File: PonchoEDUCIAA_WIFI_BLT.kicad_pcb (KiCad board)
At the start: 2 copper layers, 21 parts, among them J1 UART, SW1 Reset, SW2 Boot, U1 ESP32-WROOM

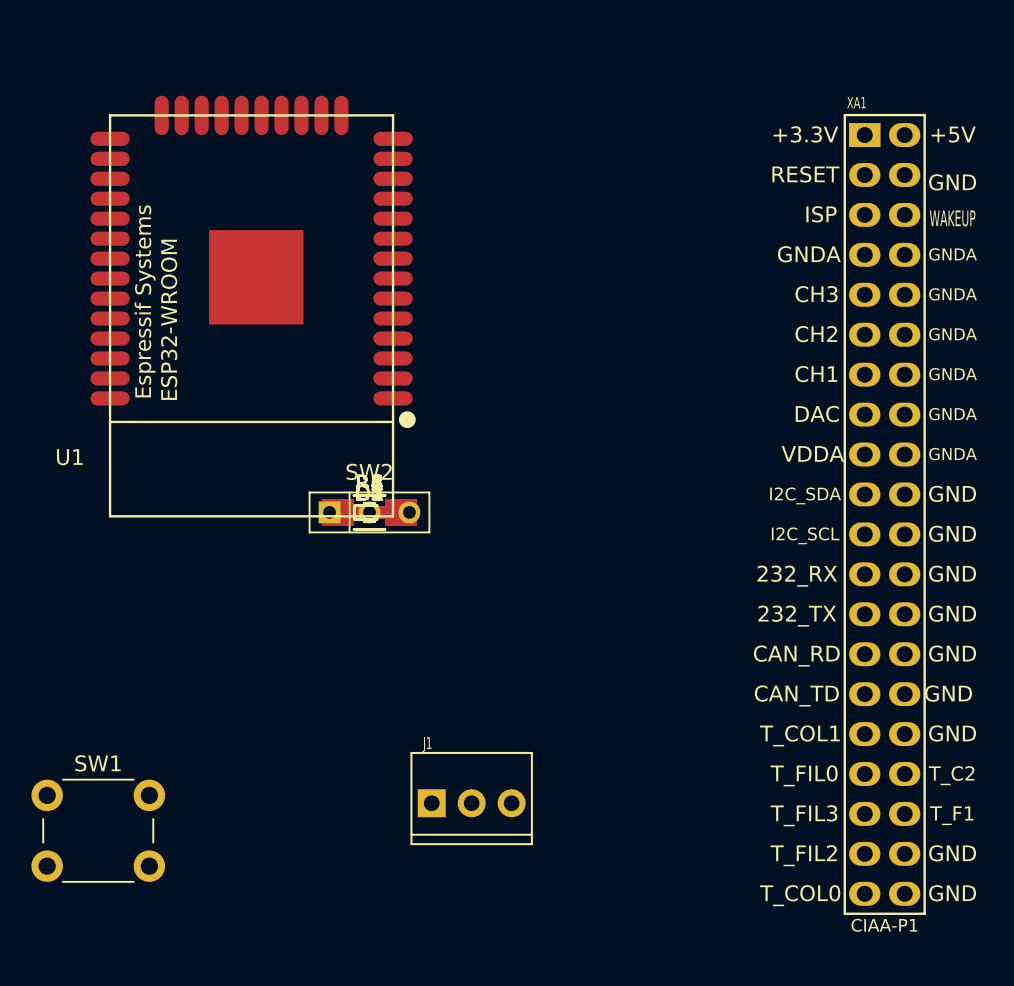
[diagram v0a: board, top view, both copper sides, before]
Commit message: Se distribuyen los componentes en el PCB
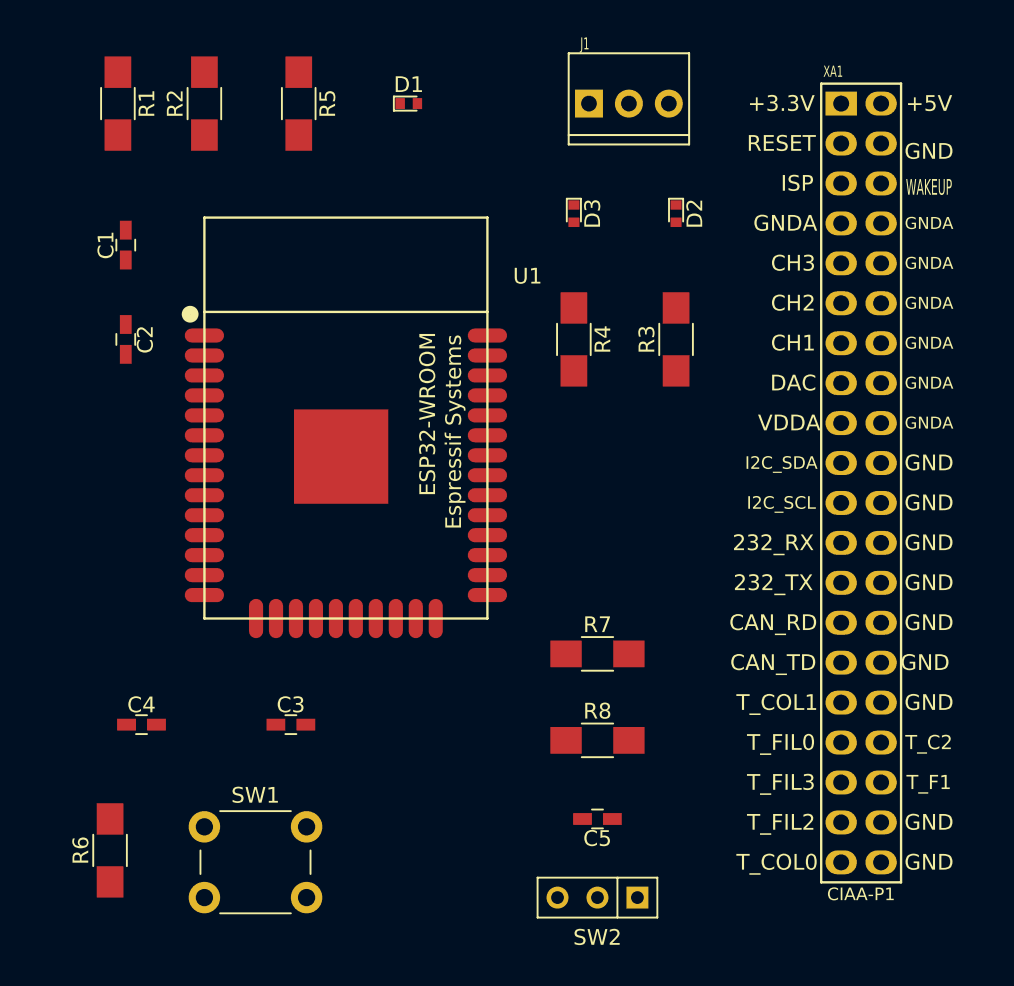
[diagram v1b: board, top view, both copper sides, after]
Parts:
- moved J1 45.6 mm to (165.0, 79.0)
- moved R1 30.5 mm to (132.5, 79.0), turned to 270 degrees
- moved SW2 28.5 mm to (163.0, 129.5), turned to 180 degrees
- moved R2 28.0 mm to (138.0, 79.0), turned to 90 degrees
- moved D2 27.2 mm to (168.0, 86.0), turned to 270 degrees
- moved R6 27.1 mm to (132.0, 126.5), turned to 90 degrees
- moved R5 26.4 mm to (144.0, 79.0), turned to 270 degrees
- moved D1 26.1 mm to (151.0, 79.0)
- moved C5 24.3 mm to (163.0, 124.5), turned to 180 degrees
- moved D3 23.0 mm to (161.5, 86.0), turned to 270 degrees
- moved C1 23.0 mm to (133.0, 88.0), turned to 90 degrees
- moved R3 22.4 mm to (168.0, 94.0), turned to 90 degrees
- moved R8 20.5 mm to (163.0, 119.5)
- moved C4 19.8 mm to (134.0, 118.5)
- moved C2 19.0 mm to (133.0, 94.0), turned to 270 degrees
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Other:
- net class Default: clearance 0.2 -> 0.3; trace_width 0.25 -> 0.3; via_dia 0.6 -> 1.27; via_drill 0.4 -> 0.7
- rule trace_clearance: 0.2 -> 0.3

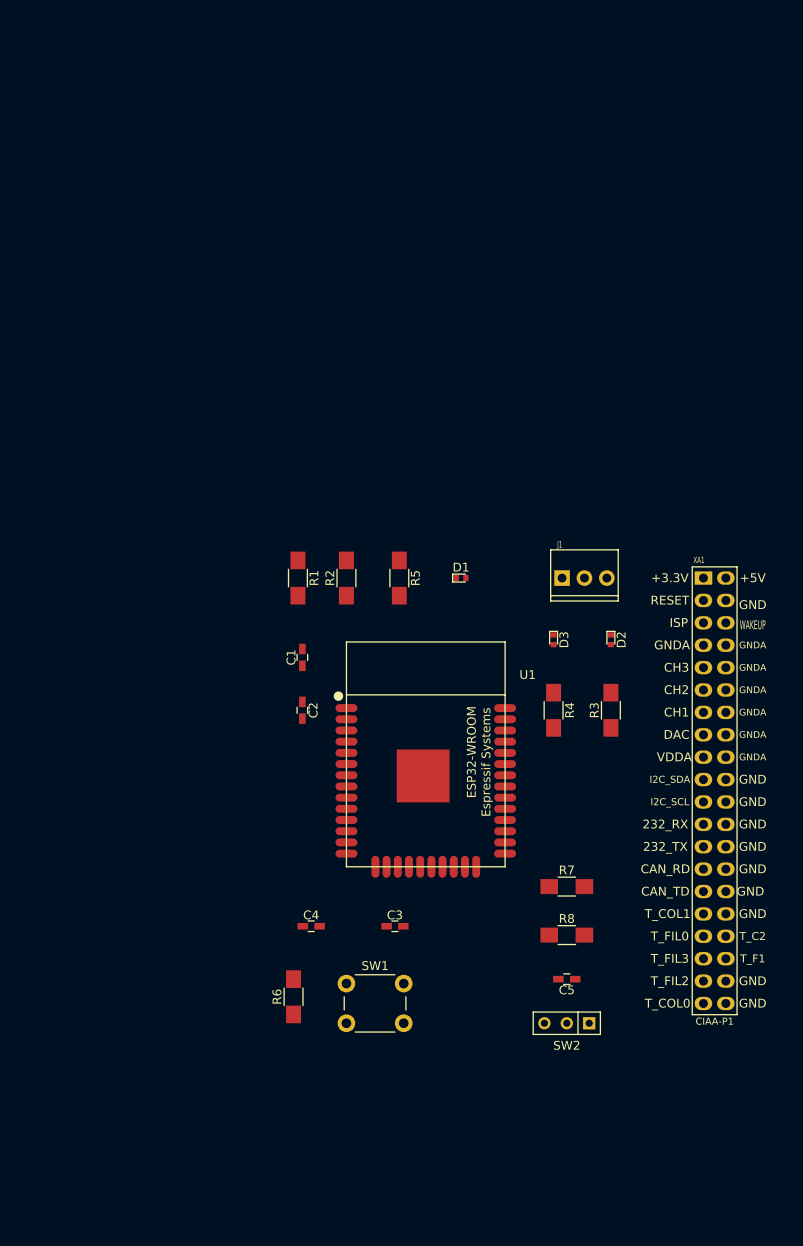
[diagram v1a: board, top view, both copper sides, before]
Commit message: Se agregan modelos 3d al proyecto y datashets de algunos componentes
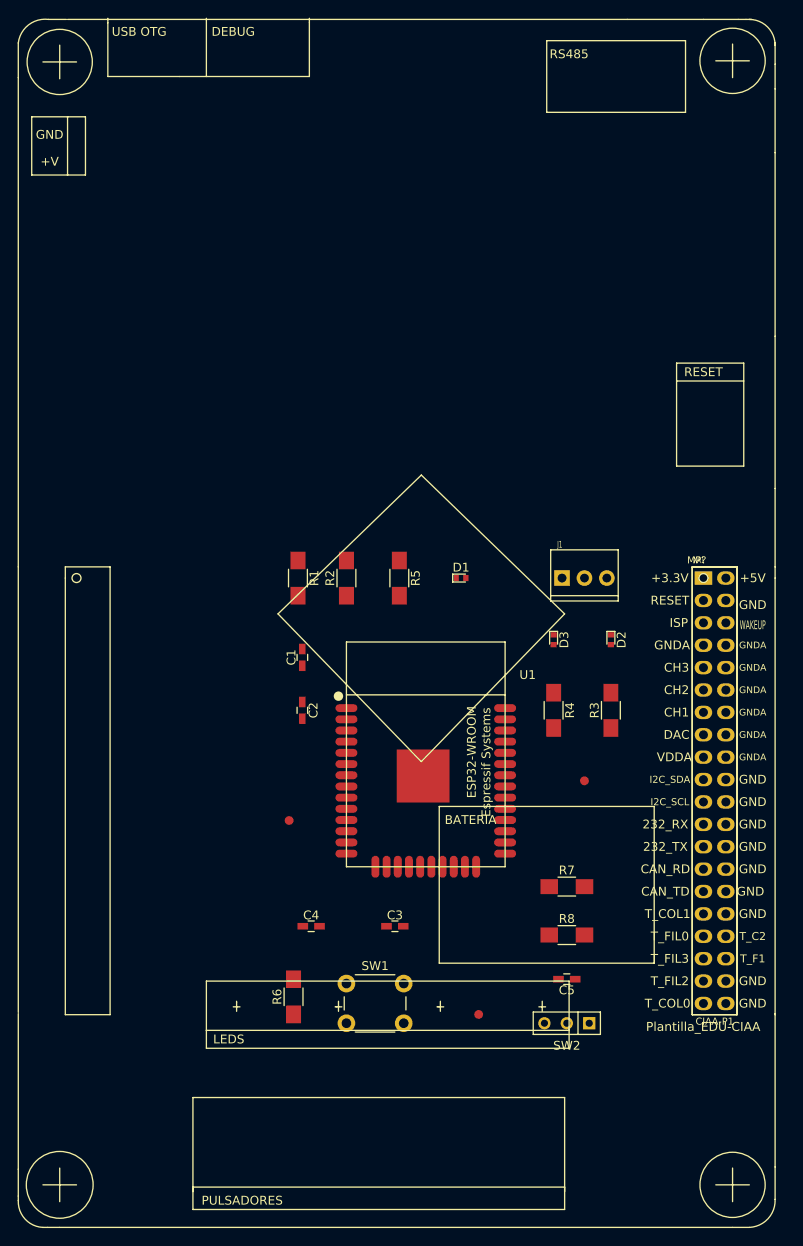
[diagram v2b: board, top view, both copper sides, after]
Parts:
- added F1: FIDUCIAL, PonchoEDUCIAA_WIFI_BLTH:Fiducial_1mm, F.Cu at (153.0, 128.5)
- added F2: FIDUCIAL, PonchoEDUCIAA_WIFI_BLTH:Fiducial_1mm, F.Cu at (131.5, 106.5)
- added F3: FIDUCIAL, PonchoEDUCIAA_WIFI_BLTH:Fiducial_1mm, F.Cu at (165.0, 102.0)
- added MP?: Plantilla_EDU-CIAA, PonchoEDUCIAA_WIFI_BLTH:Plantilla_EDU-CIAA, F.Cu at (178.5, 79.0)
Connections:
- R3 pad 1: Net-(D2-Pad2) -> Net-(J1-Pad1)
- R3 pad 2: Net-(J1-Pad1) -> Net-(D2-Pad2)
- R4 pad 1: Net-(D3-Pad2) -> Net-(J1-Pad2)
- R4 pad 2: Net-(J1-Pad2) -> Net-(D3-Pad2)

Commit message: Se incorpora el nuevo netlist al pcb
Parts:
- C1: value 0,1uF/10V -> 0,1uF
- C2: value 10uF/6,3V -> 10uF
- C3: value 1nF/50V -> 1nF
- C4: value 0,1nF/50V -> 0,1nF
- C5: value 1nF/10V -> 1nF
- R2: value 400 -> 10k
- R3: value 400 -> 470
- R5: value 10k -> 400
- R8: value 470 -> 5k
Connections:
- C1 pad 2: Net-(C1-Pad2) -> +3V3
- C2 pad 2: Net-(C1-Pad2) -> +3V3
- R1 pad 1: +3V3 -> Net-(D1-Pad2)
- R1 pad 2: Net-(C1-Pad2) -> +3V3
- R2 pad 1: Net-(D1-Pad2) -> +3V3
- R2 pad 2: +3V3 -> Net-(C4-Pad1)
- R3 pad 1: Net-(J1-Pad1) -> Net-(C3-Pad1)
- R3 pad 2: Net-(D2-Pad2) -> Net-(C4-Pad1)
- R5 pad 1: +3V3 -> Net-(J1-Pad1)
- R5 pad 2: Net-(C4-Pad1) -> Net-(D2-Pad2)
- R6 pad 1: Net-(C3-Pad1) -> Net-(C5-Pad2)
- R6 pad 2: Net-(C4-Pad1) -> Net-(R6-Pad2)
- R7 pad 2: Net-(R7-Pad2) -> Net-(R6-Pad2)
- R8 pad 1: Net-(C5-Pad2) -> GND
- R8 pad 2: Net-(R7-Pad2) -> Net-(R8-Pad2)
- U1 pad 2: Net-(C1-Pad2) -> +3V3
- U1 pad 24: GND -> Net-(R8-Pad2)
- U1 pad 25: Net-(R7-Pad2) -> Net-(R6-Pad2)

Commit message: Revision del proyecto
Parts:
- removed MP?: Plantilla_EDU-CIAA, PonchoEDUCIAA_WIFI_BLTH:Plantilla_EDU-CIAA
- added G1: WIFI-BLTH, PonchoEDUCIAA_WIFI_BLTH:Logo_Poncho, F.Cu at (148.0, 121.5)
- R1, R4, R5: value 400 -> 402
- moved R6 36.9 mm to (165.5, 111.0), turned to 180 degrees
- moved R3 32.4 mm to (139.0, 79.5)
- moved R5 28.3 mm to (168.0, 94.0)
- moved F3 25.6 mm to (157.5, 77.5)
- moved F1 19.2 mm to (172.0, 131.0)
- moved C3 10.1 mm to (133.5, 120.0)
- moved R7 9.34 mm to (165.5, 105.0)
- moved R2 7.02 mm to (145.0, 79.5)
- moved C5 6.96 mm to (165.5, 118.0)
- moved SW1 4.53 mm to (133.5, 125.5)
- moved R8 4.03 mm to (159.0, 119.0), turned to 90 degrees
- moved C4 3.54 mm to (133.5, 115.0)
- moved D1 1.12 mm to (152.0, 79.5)
- moved D2 1.00 mm to (169.0, 86.0)
- moved D3 1.00 mm to (162.5, 86.0)
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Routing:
- net Net-(J1-Pad1): track 0.00 -> 63.2 mm
- net Net-(C3-Pad1): track 0.00 -> 60.2 mm
- net Net-(J1-Pad2): track 0.00 -> 49.2 mm
- net Net-(C4-Pad1): track 0.00 -> 48.7 mm
- net GND: track 0.00 -> 26.6 mm, vias 0 -> 12
- net Net-(C5-Pad2): track 0.00 -> 22.1 mm
- net Net-(D1-Pad2): track 0.00 -> 22.0 mm
- net Net-(R6-Pad2): track 0.00 -> 15.8 mm
- net +3V3: track 0.00 -> 14.6 mm, vias 0 -> 4
- net Net-(D2-Pad2): track 0.00 -> 11.7 mm
- net Net-(D3-Pad2): track 0.00 -> 11.3 mm
- net Net-(R8-Pad2): track 0.00 -> 9.46 mm
- added copper zone on Power, net +3V3
- added copper zone on GND, net GND
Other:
- board outline added: 57.5 x 59.5 mm
- copper layers 2 -> 4

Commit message: Primer ruteo tentativo
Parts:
- moved R3 30.0 mm to (131.5, 108.5)
- moved F2 5.00 mm to (131.5, 101.5)
- moved C4 4.03 mm to (137.5, 115.5)
- moved F3 2.50 mm to (157.5, 80.0)
- moved SW2 1.00 mm to (163.5, 130.0), turned to 0 degrees
- turned C5 to 0 degrees
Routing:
- net GND: track 26.6 -> 234.5 mm, vias 12 -> 0
- net +3V3: track 14.6 -> 120.3 mm, vias 4 -> 0
- net Net-(C3-Pad1): track 60.2 -> 27.3 mm
- net Net-(J1-Pad2): track 49.2 -> 66.1 mm
- net Net-(J1-Pad1): track 63.2 -> 68.9 mm
- net Net-(C5-Pad2): track 22.1 -> 19.6 mm
- net Net-(C4-Pad1): track 48.7 -> 49.7 mm
- removed copper zone on Power, net +3V3
- removed copper zone on GND, net GND
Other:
- copper layers 4 -> 2
- rule trace_min: 0.2 -> 0.25

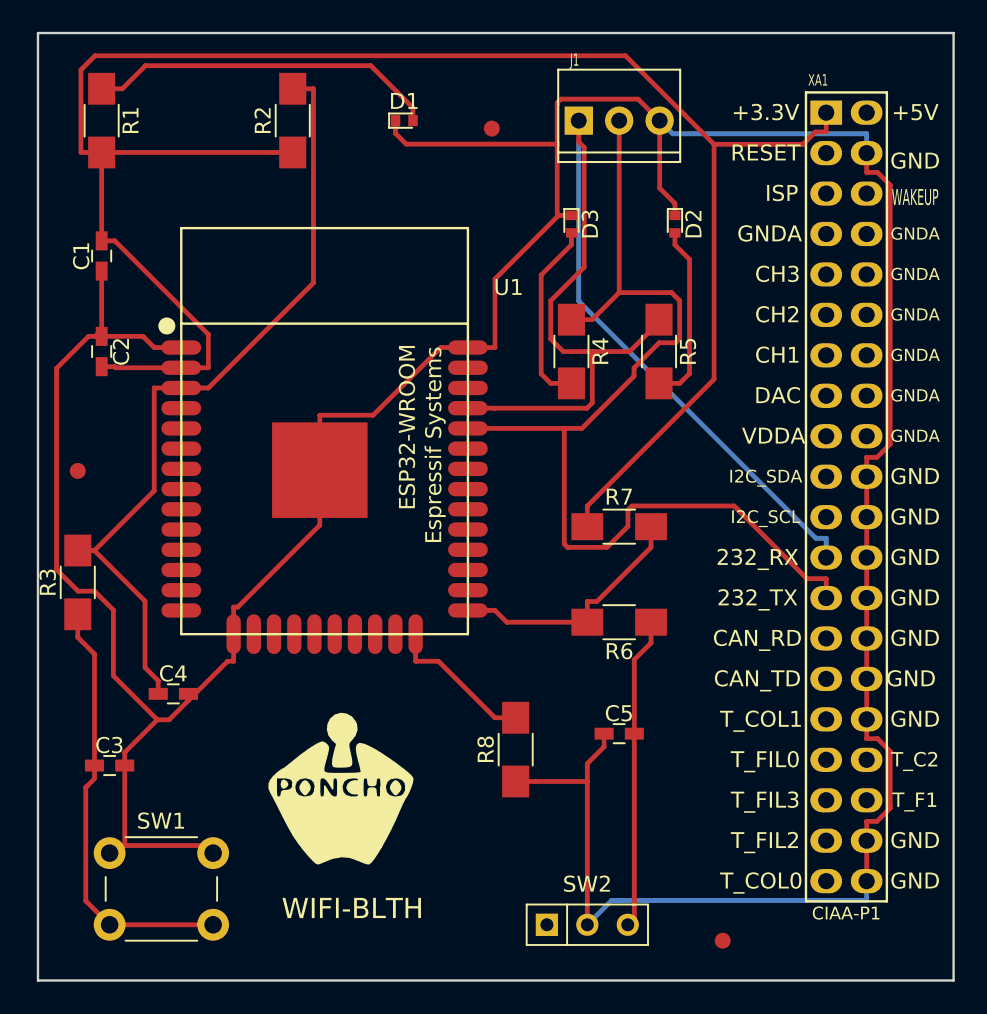
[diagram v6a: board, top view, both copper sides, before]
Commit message: Rediseño de las conexiones del pcb
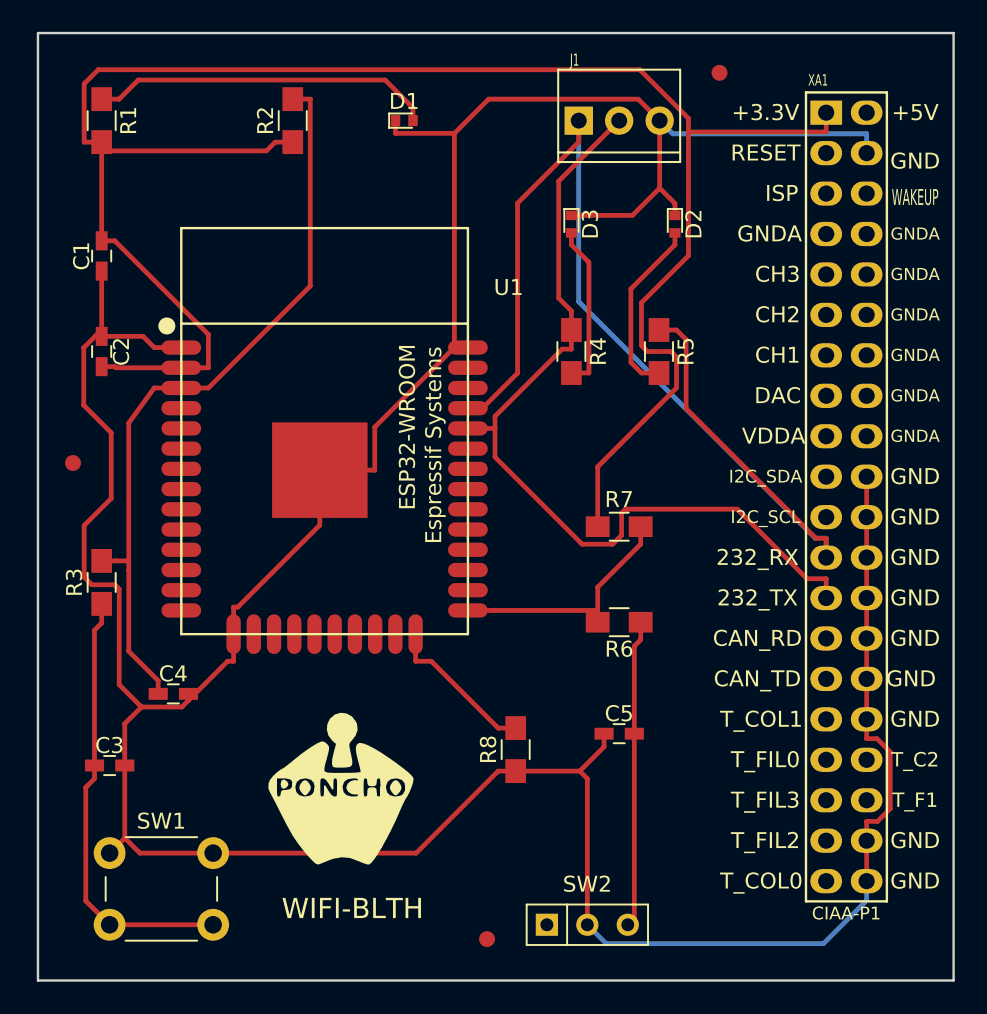
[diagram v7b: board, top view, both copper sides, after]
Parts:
- R1, R2, R3, R4, R5, R6, R7, R8: footprint Resistors_SMD:R_1206_HandSoldering -> Resistors_SMD:R_0805_HandSoldering
- moved F1 14.8 mm to (157.2, 130.9)
- moved F3 14.7 mm to (171.8, 76.5)
- moved R3 1.50 mm to (133.0, 108.5)
- moved F2 0.58 mm to (131.2, 101.0)
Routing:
- net Net-(J1-Pad2): track 66.1 -> 54.9 mm
- net Net-(J1-Pad1): track 68.9 -> 75.4 mm
- net Net-(C4-Pad1): track 49.7 -> 47.5 mm
- net Net-(D3-Pad2): track 11.8 -> 10.4 mm
- net +3V3: track 120.3 -> 121.5 mm
- net Net-(R6-Pad2): track 15.8 -> 15.3 mm
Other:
- rule via_min_drill: 0.3 -> 0.4
- rule via_min_size: 0.4 -> 0.8
